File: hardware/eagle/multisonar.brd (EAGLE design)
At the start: 96 x 96 mm, 23 parts, among them IC1 ATMEGA328-20P, J1 ARDUINO_R3_SHIELD, Y1 16MHZ

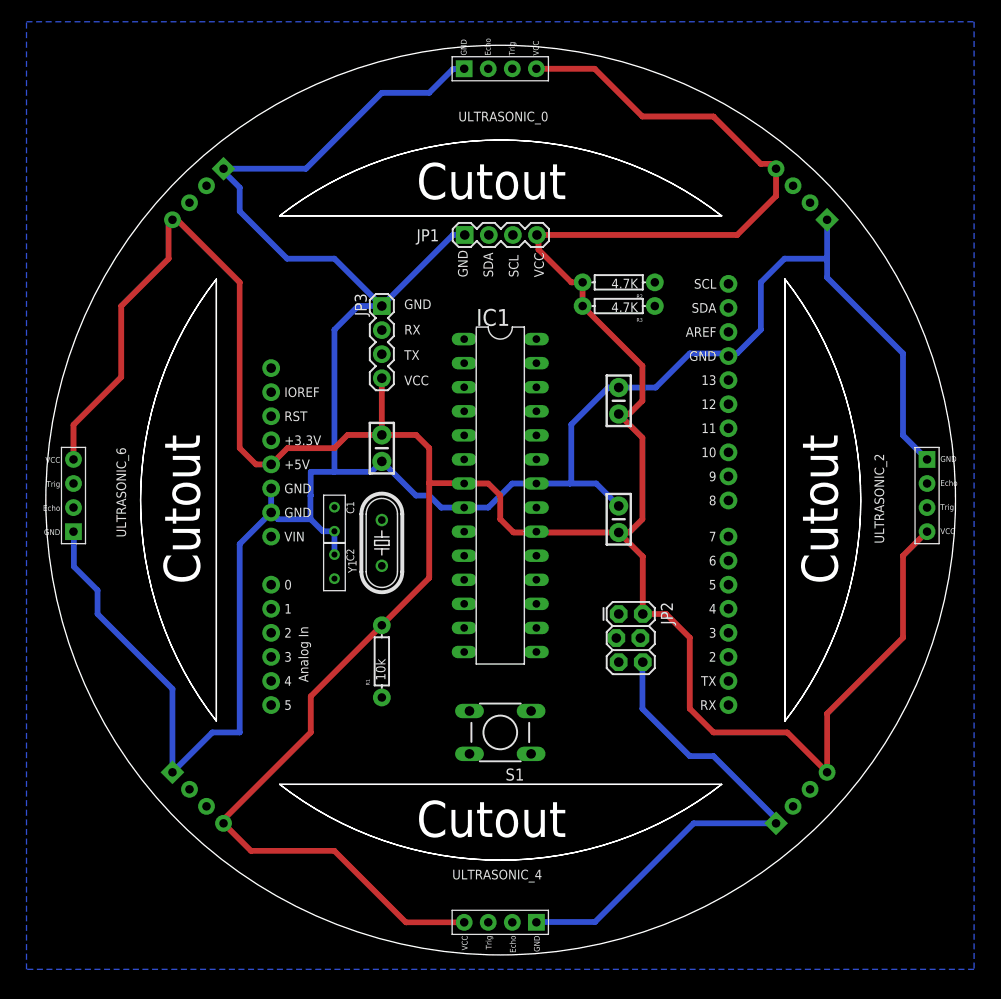
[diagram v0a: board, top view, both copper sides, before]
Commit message: Routed all components
TO-DO: Add silk screen
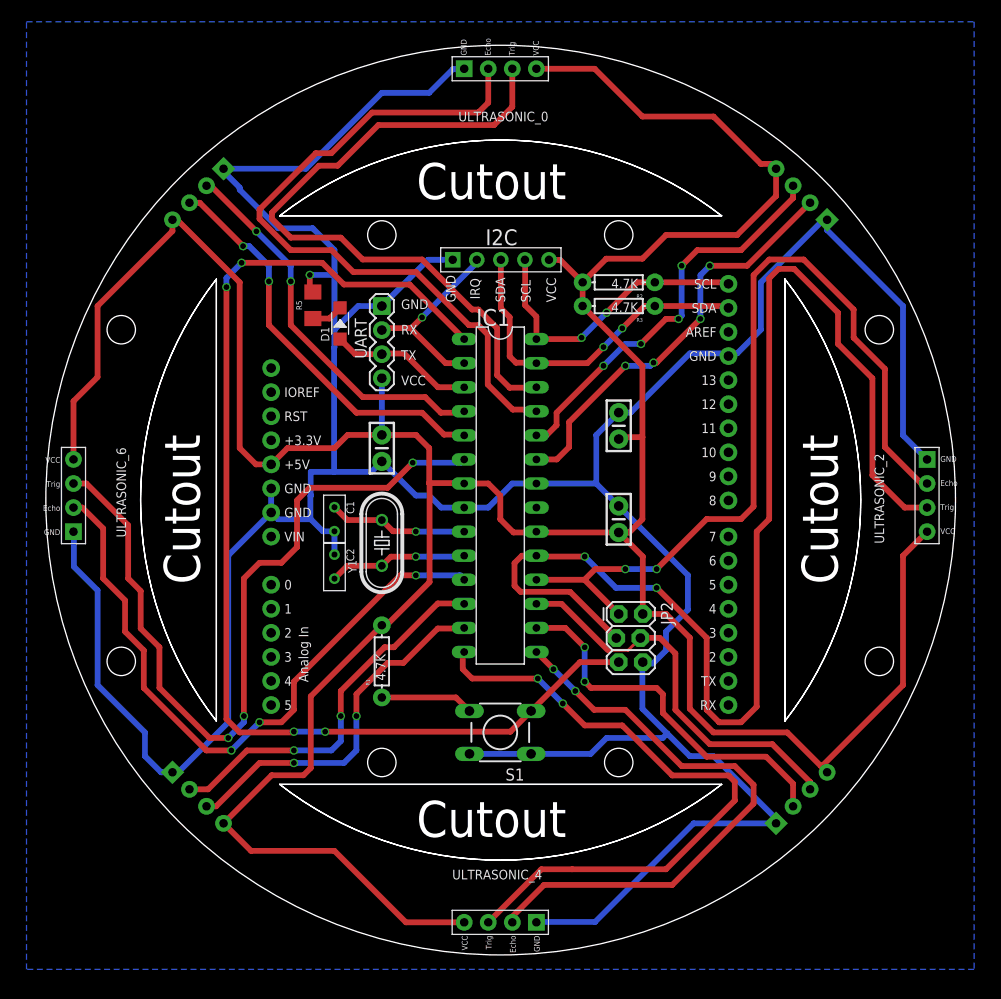
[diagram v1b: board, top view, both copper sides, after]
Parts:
- removed JP1: (no value), SparkFun-Connectors:1X04
- added D1: (no value), Seeed-OPL-Diode:SOD-123
- added I2C: 5p-2.54, Seeed-OPL-Connector:H5-2.54
- added R5: 220, SparkFun-Resistors:1206
- R1: value 10k -> 4.7K
- moved C5 2.64 mm to (95.0, 57.4)
- renumbered JP3 to UART
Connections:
- removed net RX: IC1.2, UART.2
- removed net TX: IC1.3, UART.3
- new net N$1: R1.P$1, S1.4
- new net N$2: D1.-, R5.1
- new net RX/IRQ: I2C.2, IC1.2, UART.2
- new net TX/LED: D1.+, IC1.3, UART.3
- net GND: now also I2C.1, R5.2, S1.2; no longer JP1.1
- net PB0: now also ULTRASONIC_4.TRIG; no longer ULTRASONIC_5.ECHO
- net PB1: now also ULTRASONIC_4.ECHO; no longer ULTRASONIC_5.TRIG
- net PB2: now also ULTRASONIC_3.ECHO; no longer ULTRASONIC_6.ECHO
- net PB3: now also ULTRASONIC_3.TRIG; no longer ULTRASONIC_6.TRIG
- net PB4: now also ULTRASONIC_2.ECHO; no longer ULTRASONIC_7.ECHO
- net PB5: now also ULTRASONIC_2.TRIG; no longer ULTRASONIC_7.TRIG
- net PC0: now also ULTRASONIC_1.ECHO; no longer ULTRASONIC_0.ECHO
- net PC1: now also ULTRASONIC_1.TRIG; no longer ULTRASONIC_0.TRIG
- net PC2: now also ULTRASONIC_0.ECHO; no longer ULTRASONIC_1.ECHO
- net PC3: now also ULTRASONIC_0.TRIG; no longer ULTRASONIC_1.TRIG
- net PD2: now also ULTRASONIC_7.ECHO; no longer ULTRASONIC_2.ECHO
- net PD3: now also ULTRASONIC_7.TRIG; no longer ULTRASONIC_2.TRIG
- net PD4: now also ULTRASONIC_6.TRIG; no longer ULTRASONIC_3.ECHO
- net PD5: now also ULTRASONIC_6.ECHO; no longer ULTRASONIC_3.TRIG
- net PD6: now also ULTRASONIC_5.ECHO; no longer ULTRASONIC_4.ECHO
- net PD7: now also ULTRASONIC_5.TRIG; no longer ULTRASONIC_4.TRIG
- net RST: no longer R1.P$1
- net SCL: now also I2C.4; no longer JP1.3
- net SDA: now also I2C.3; no longer JP1.2
- net VCC: now also I2C.5; no longer JP1.4
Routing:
- net PB5: track 0.00 -> 134.9 mm, vias 0 -> 2
- net RST: track 0.00 -> 120.7 mm, vias 0 -> 4
- net PB4: track 0.00 -> 91.0 mm, vias 0 -> 2
- net PD4: track 0.00 -> 84.4 mm, vias 0 -> 3
- net PC2: track 0.00 -> 74.1 mm
- net PC3: track 0.00 -> 72.9 mm
- net PB0: track 0.00 -> 68.8 mm, vias 0 -> 2
- net PD5: track 0.00 -> 68.8 mm, vias 0 -> 3
- net PB1: track 0.00 -> 61.7 mm, vias 0 -> 2
- net PC0: track 0.00 -> 44.4 mm, vias 0 -> 4
- net GND: track 332.2 -> 375.8 mm, vias 0 -> 1
- net PD3: track 0.00 -> 42.8 mm, vias 0 -> 2
- net PC1: track 0.00 -> 42.6 mm, vias 0 -> 4
- net PB3: track 0.00 -> 42.0 mm
- net PD2: track 0.00 -> 40.8 mm, vias 0 -> 2
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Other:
- board text added: "IRQ"

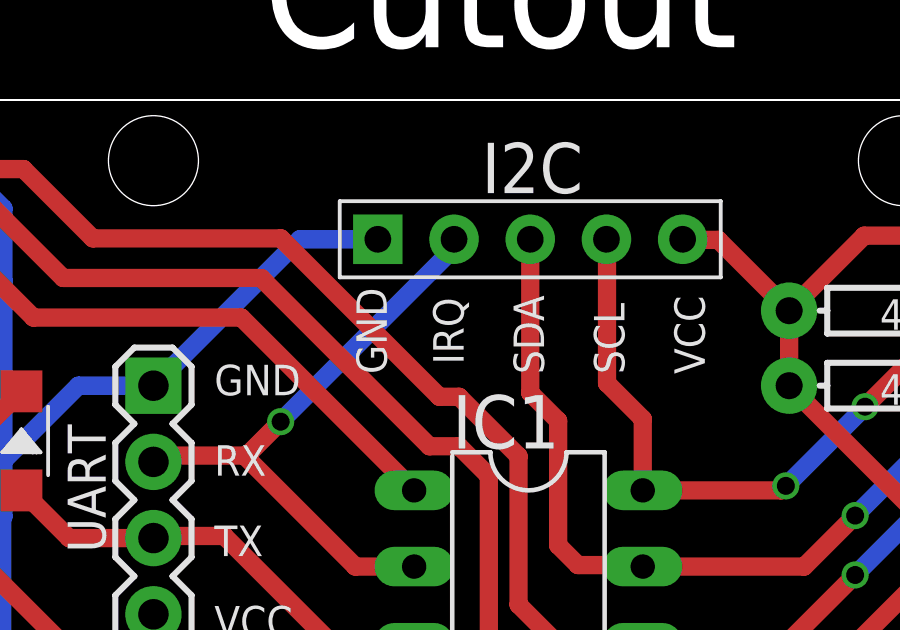
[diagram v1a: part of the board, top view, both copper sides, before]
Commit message: Change IRQ to INT for clarity
It should be easier to explain to novice users
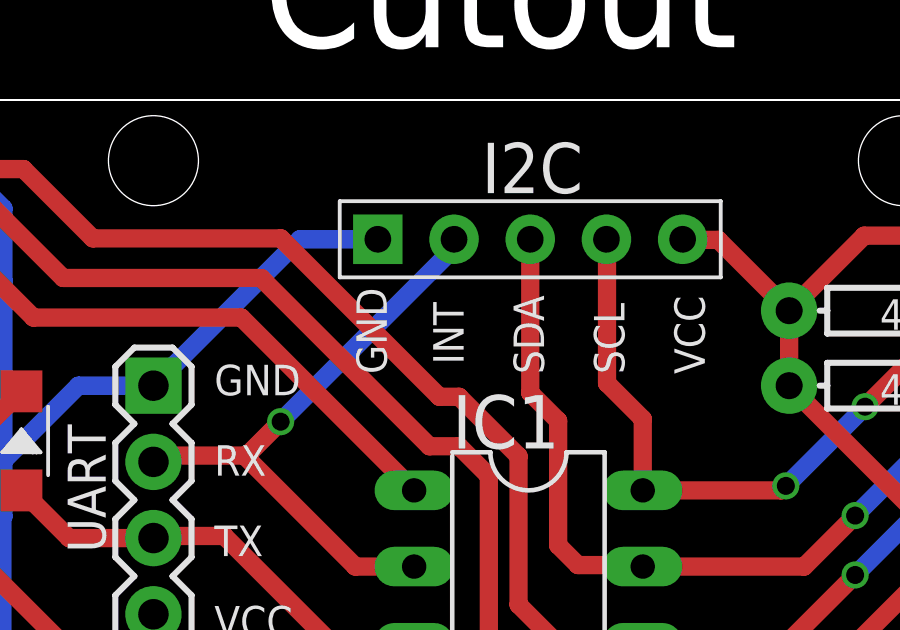
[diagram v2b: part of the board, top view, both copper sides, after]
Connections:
- net RX/IRQ renamed RX/INT
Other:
- board text added: "INT"
- board text removed: "IRQ"
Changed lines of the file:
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@@
 <hole x="122.5" y="67.5" drill="3"/>
 <hole x="42.5" y="67.5" drill="3"/>
-<text x="80.34" y="70.71" size="1.016" layer="21" font="vector" rot="R90">IRQ</text>
+<text x="80.34" y="70.71" size="1.016" layer="21" font="vector" rot="R90">INT</text>
 </plain>
 <attributes>
@@
 <wire x1="111.87" y1="73.92" x2="110.88" y2="72.93" width="0.6096" layer="1"/>
 </signal>
-<signal name="RX/IRQ">
+<signal name="RX/INT">
 <contactref element="UART" pad="2"/>
 <contactref element="IC1" pad="2"/>

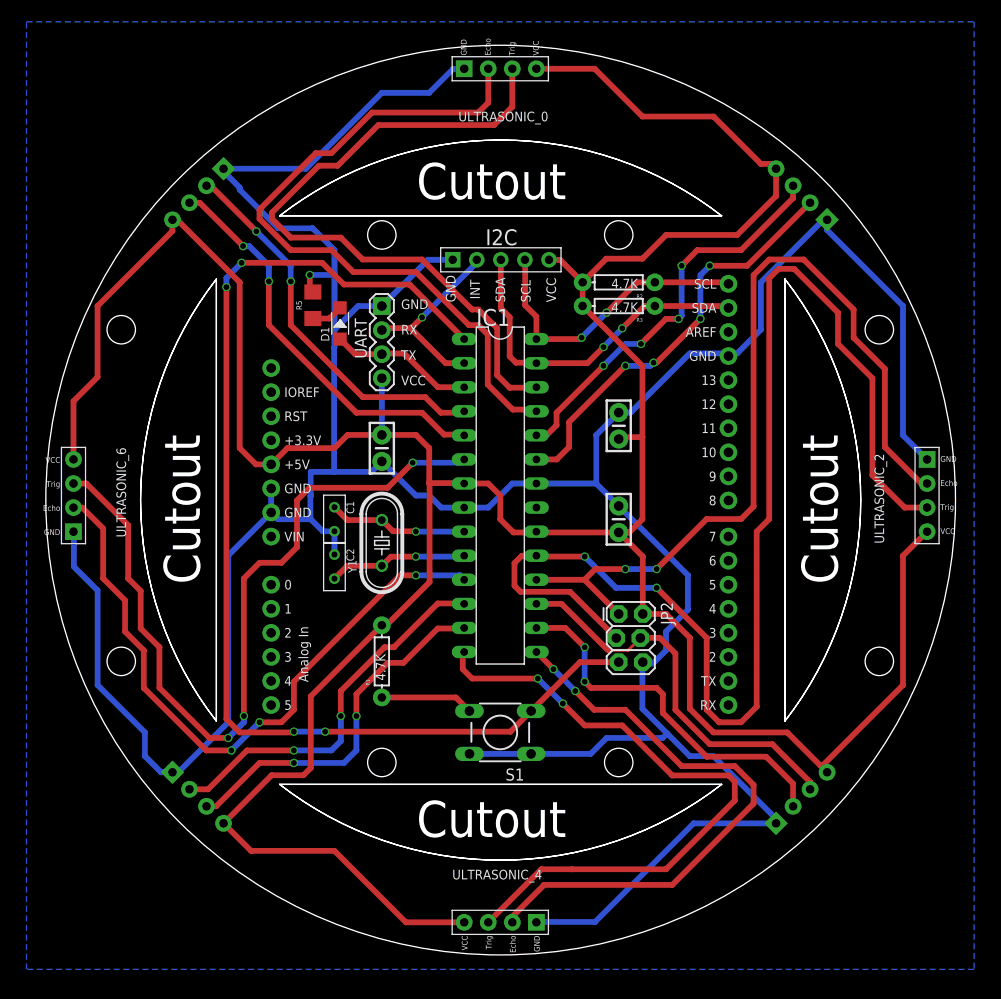
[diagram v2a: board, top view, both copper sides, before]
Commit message: Add bottom silk screen
Board Rev. 0, sent to PCBWay
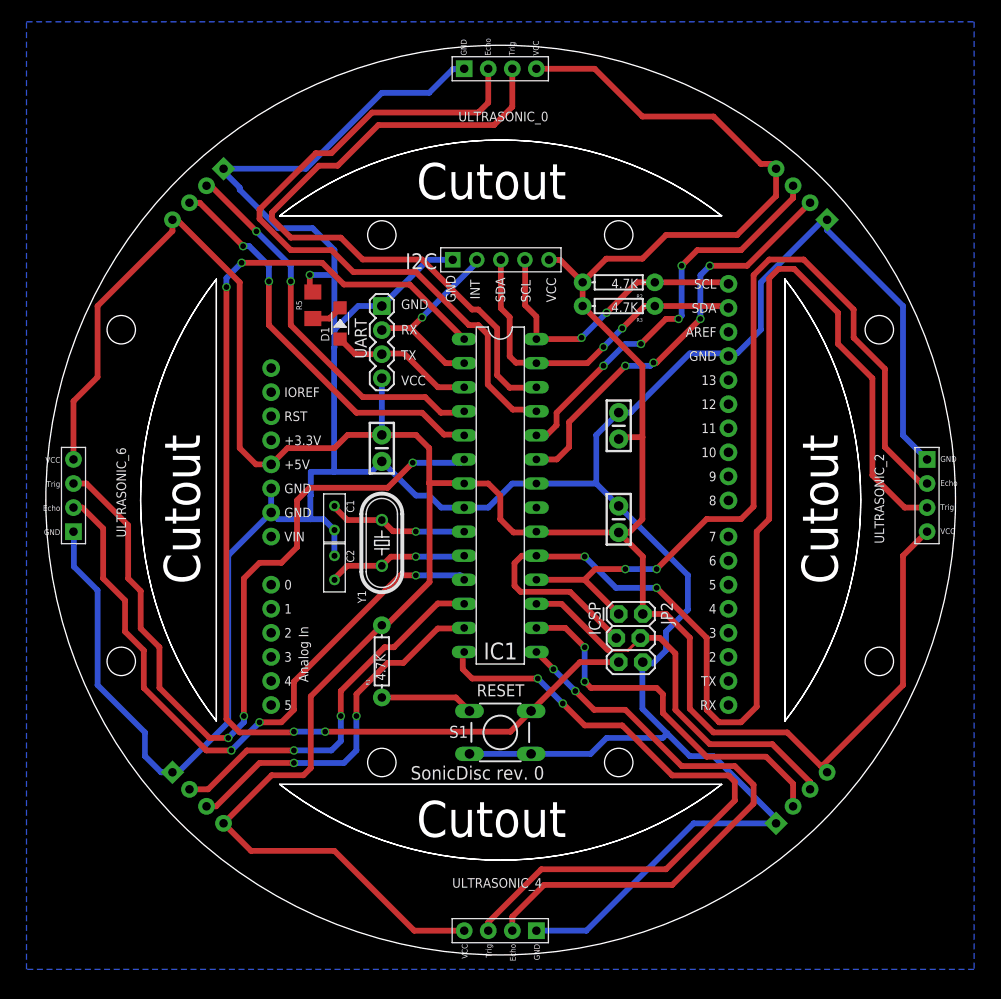
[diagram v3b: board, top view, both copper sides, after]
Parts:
- moved ULTRASONIC_4 0.88 mm to (82.5, 6.62)
- moved C1 0.13 mm to (65.0, 47.6)
- moved C2 0.13 mm to (65.0, 42.4)
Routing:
- net PB1: track 61.7 -> 62.6 mm
- net PB0: track 68.8 -> 69.7 mm
- net GND: track 375.8 -> 376.3 mm
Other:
- board text added: "SonicDisc rev. 0"

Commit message: Increase board size to 99mm
Fixes #1
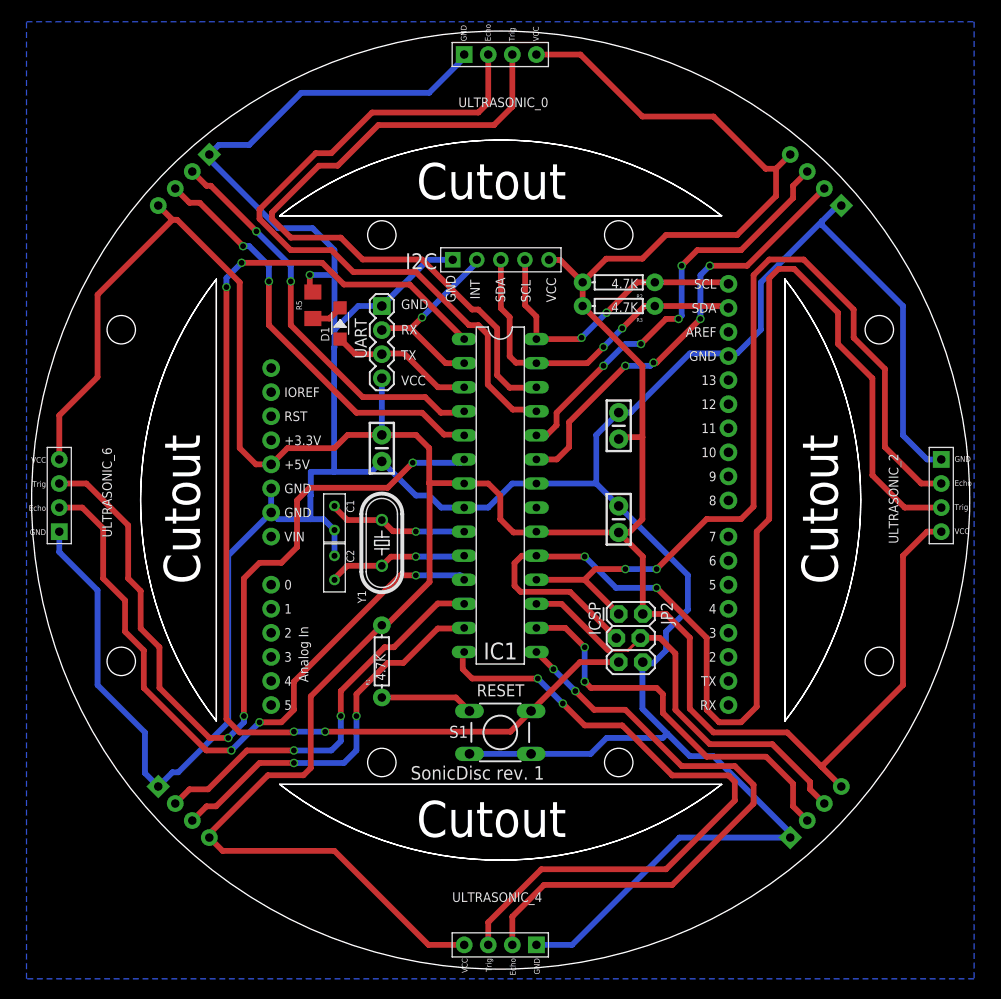
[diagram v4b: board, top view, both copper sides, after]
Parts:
- moved ULTRASONIC_1 2.12 mm to (114.0, 81.5)
- moved ULTRASONIC_3 2.12 mm to (114.0, 18.4)
- moved ULTRASONIC_5 2.12 mm to (50.9, 18.4)
- moved ULTRASONIC_7 2.12 mm to (50.9, 81.5)
- moved ULTRASONIC_0 1.50 mm to (82.5, 94.0)
- moved ULTRASONIC_2 1.50 mm to (126.5, 50.0)
- moved ULTRASONIC_4 1.50 mm to (82.5, 5.12)
- moved ULTRASONIC_6 1.50 mm to (38.5, 50.0)
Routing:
- net GND: track 376.3 -> 390.4 mm
- net VCC: track 354.6 -> 367.6 mm
- net PD6: track 40.2 -> 42.3 mm
- net PD3: track 42.8 -> 45.0 mm
- net PD2: track 40.8 -> 43.0 mm
- net PC1: track 42.6 -> 44.8 mm
- net PC0: track 44.4 -> 46.5 mm
- net PD7: track 38.5 -> 40.6 mm
- net PB3: track 42.0 -> 44.1 mm
- net PB2: track 39.6 -> 41.7 mm
- net PD5: track 68.8 -> 70.3 mm
- net PC2: track 74.1 -> 75.6 mm
- net PB1: track 62.6 -> 64.1 mm
- net PB0: track 69.7 -> 71.2 mm
- net PD4: track 84.4 -> 85.9 mm
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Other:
- board size 96 x 96 mm -> 99 x 99 mm
- board text added: "SonicDisc rev. 1"
- board text removed: "SonicDisc rev. 0"

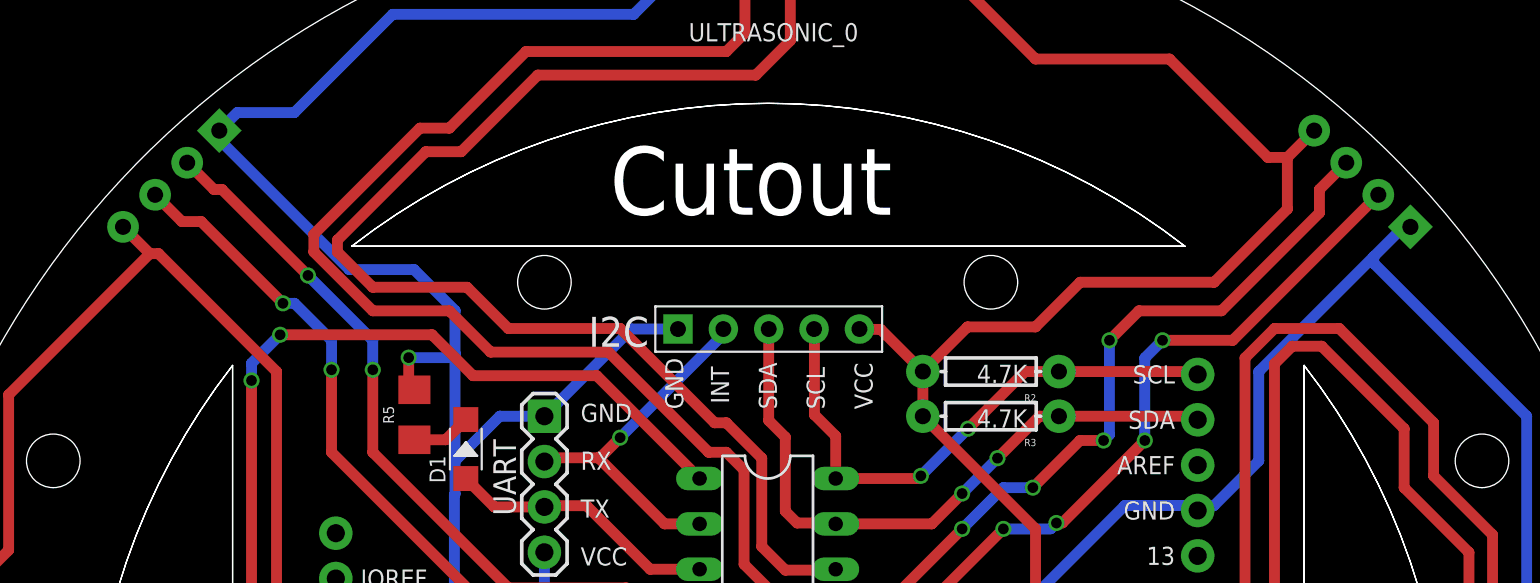
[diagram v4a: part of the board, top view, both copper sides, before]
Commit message: Moving i2c header downwards
So there is more space when angled headers are used
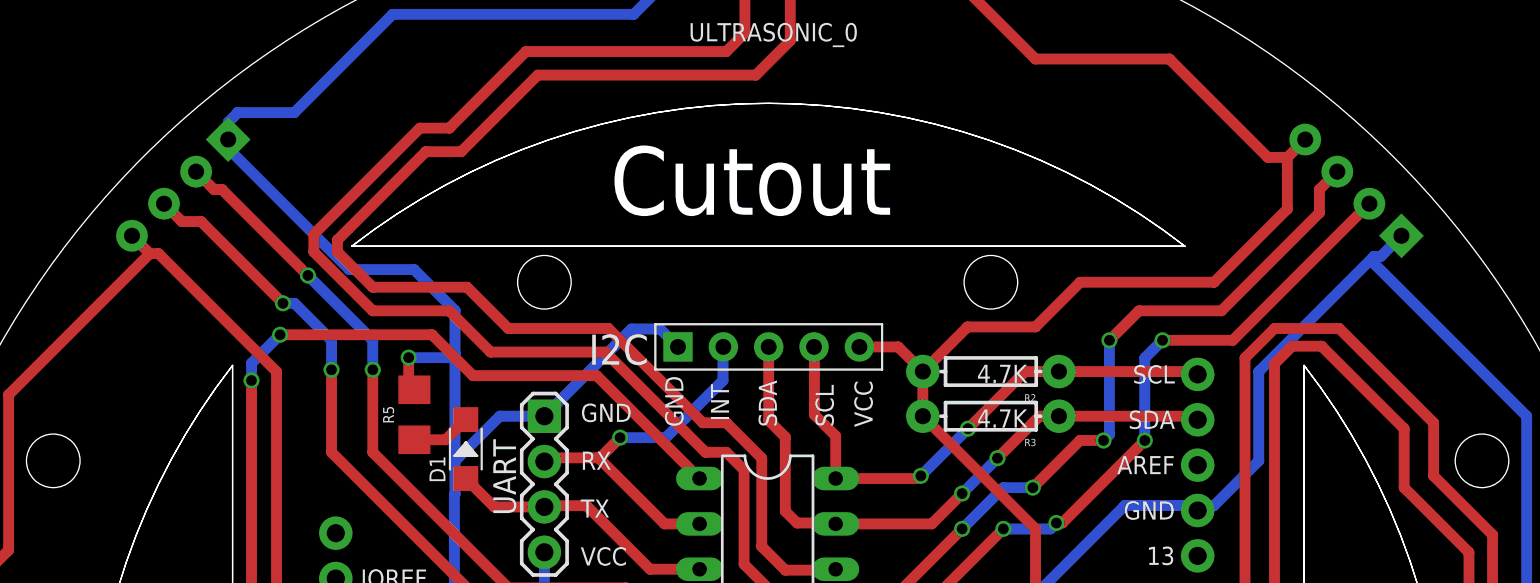
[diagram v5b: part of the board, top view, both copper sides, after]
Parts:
- moved I2C 1.00 mm to (82.6, 73.9)
- moved ULTRASONIC_1 0.71 mm to (113.5, 81.0)
- moved ULTRASONIC_7 0.71 mm to (51.4, 81.0)
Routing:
- net VCC: track 367.6 -> 365.7 mm
- net SDA: track 36.6 -> 35.6 mm
- net SCL: track 31.7 -> 30.7 mm
- net PD3: track 45.0 -> 44.2 mm
- net PD2: track 43.0 -> 42.3 mm
- net PC1: track 44.8 -> 44.0 mm
- net PC0: track 46.5 -> 45.8 mm
